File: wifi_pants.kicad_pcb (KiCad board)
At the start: 2 copper layers, 65 x 30 mm, 77 parts, among them P1 CONN_02X20, U1 ESP-12E

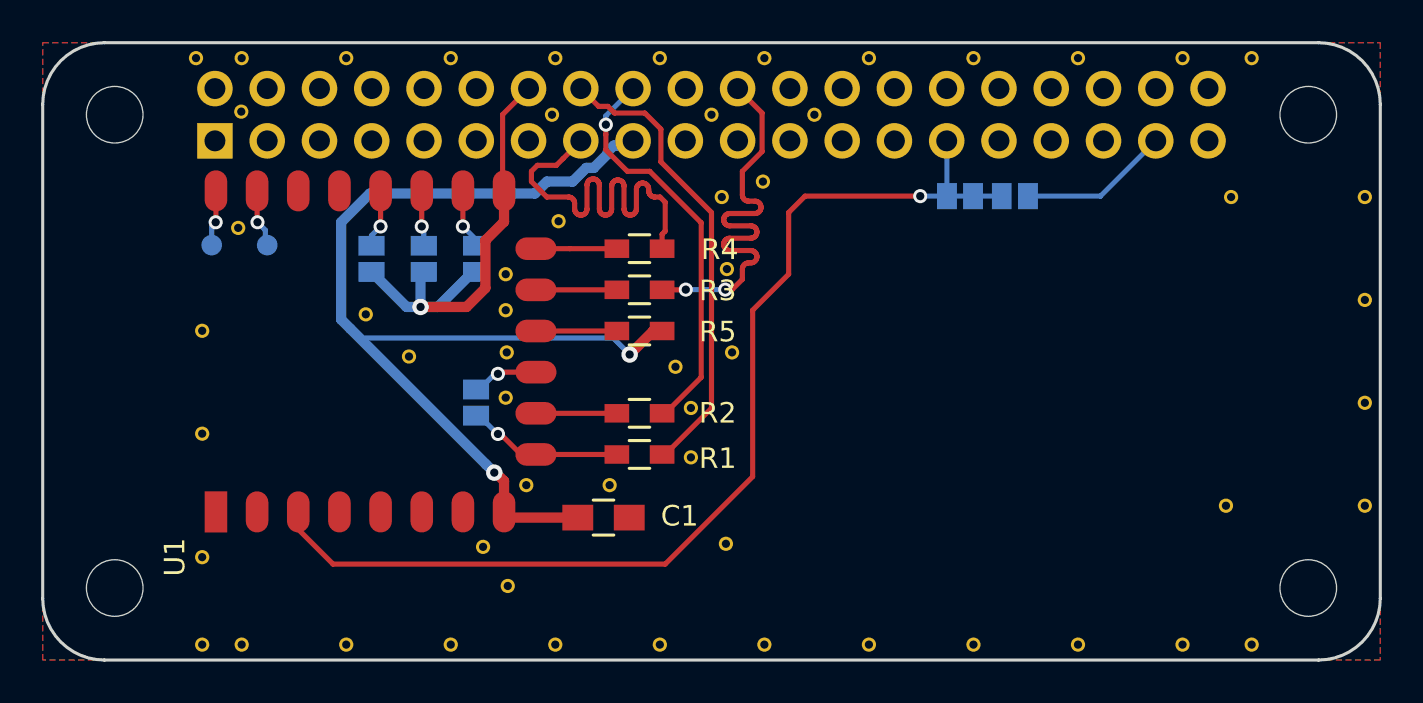
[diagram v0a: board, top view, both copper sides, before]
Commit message: Add UART header, clean up routing
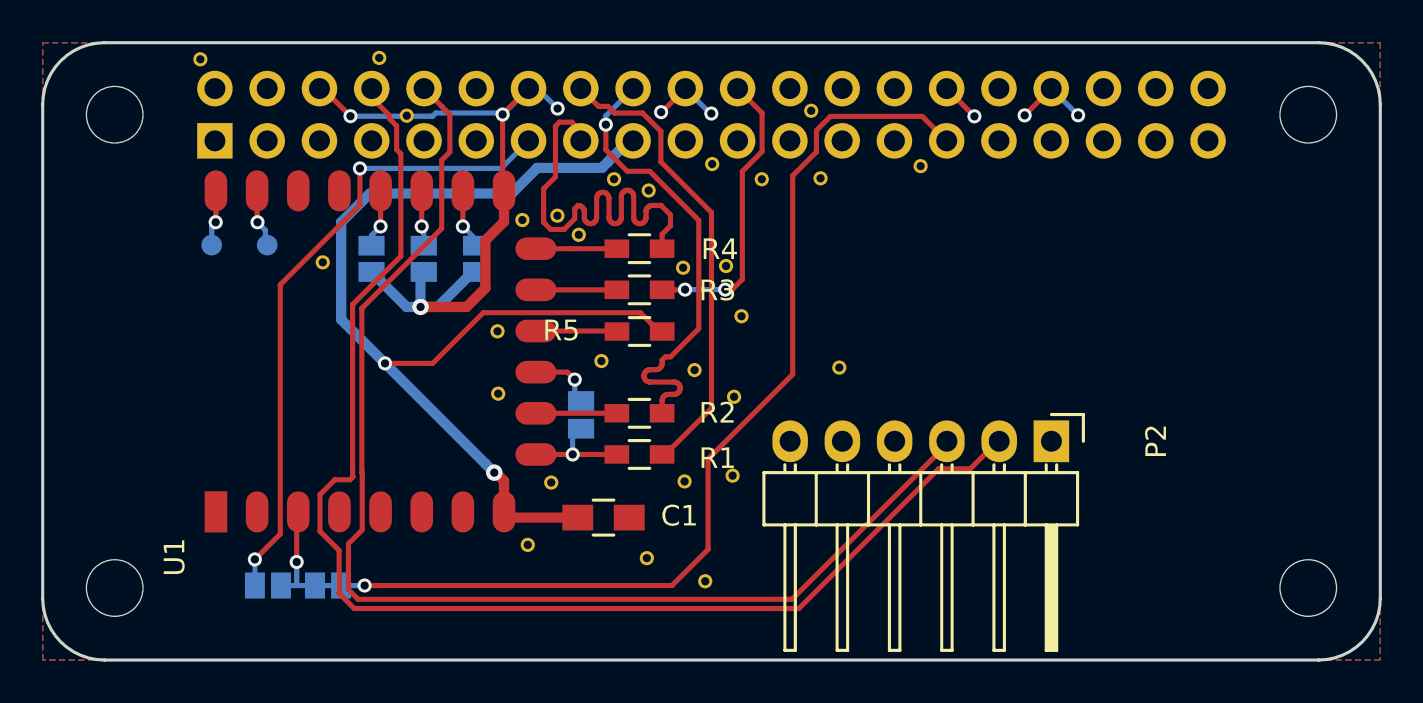
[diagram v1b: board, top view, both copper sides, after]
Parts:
- removed the REF** at (86.4, 109.5)
- removed the REF** at (87.5, 102.2)
- removed the REF** at (87.5, 98.0)
- removed the REF** at (87.5, 96.2)
- removed the REF** at (95.8, 100.8)
- removed the REF** at (96.5, 105.2)
- removed the REF** at (98.5, 100.0)
- removed the REF** at (100.0, 91.8)
- removed the REF** at (98.2, 96.0)
- removed the REF** at (89.8, 88.5)
- removed the REF** at (98.0, 92.5)
- removed the REF** at (87.6, 111.4)
- removed the REF** at (102.5, 88.5)
- removed the REF** at (97.5, 88.5)
- removed the REF** at (98.2, 109.3)
- removed the REF** at (92.5, 106.5)
- removed the REF** at (87.5, 100.0)
- removed the REF** at (82.8, 100.2)
- removed the REF** at (80.7, 98.2)
- removed the REF** at (96.5, 102.8)
- removed the REF** at (88.5, 106.5)
- removed REF**11101 (x2), REF**1111 (x2), REF**11111 (x2), REF**1121 (x2), REF**1131 (x3), REF**1141 (x2), REF**1151 (x2), REF**1161 (x2), REF**1171 (x2), REF**1181 (x2), REF**1191 (x2), REF**12, REF**13 (x5), REF**14 (x6), REF**15: VIA_0.40mm, wifi_pants:VIA_0.40mm
- added P2: CONN_01X06, Pin_Headers:Pin_Header_Angled_1x06, F.Cu at (114.0, 104.4)
- added REF**: VIA_0.40mm, wifi_pants:VIA_0.40mm, F.Cu at (97.2, 111.2)
- added REF**: VIA_0.40mm, wifi_pants:VIA_0.40mm, F.Cu at (81.4, 85.7)
- added REF**: VIA_0.40mm, wifi_pants:VIA_0.40mm, F.Cu at (102.3, 88.3)
- added REF**: VIA_0.40mm, wifi_pants:VIA_0.40mm, F.Cu at (99.9, 91.6)
- added REF**: VIA_0.40mm, wifi_pants:VIA_0.40mm, F.Cu at (103.7, 100.8)
- added REF**: VIA_0.40mm, wifi_pants:VIA_0.40mm, F.Cu at (91.1, 94.3)
- added REF**: VIA_0.40mm, wifi_pants:VIA_0.40mm, F.Cu at (94.4, 110.0)
- added REF**: VIA_0.40mm, wifi_pants:VIA_0.40mm, F.Cu at (98.6, 102.2)
- added REF**: VIA_0.40mm, wifi_pants:VIA_0.40mm, F.Cu at (98.5, 106.0)
- added REF**: VIA_0.40mm, wifi_pants:VIA_0.40mm, F.Cu at (96.2, 106.3)
- added REF**: VIA_0.40mm, wifi_pants:VIA_0.40mm, F.Cu at (89.7, 106.4)
- added REF**: VIA_0.40mm, wifi_pants:VIA_0.40mm, F.Cu at (82.7, 88.5)
- added REF**: VIA_0.40mm, wifi_pants:VIA_0.40mm, F.Cu at (87.1, 102.1)
- added REF**: VIA_0.40mm, wifi_pants:VIA_0.40mm, F.Cu at (87.1, 99.0)
- added REF**: VIA_0.40mm, wifi_pants:VIA_0.40mm, F.Cu at (88.3, 93.6)
- added REF**: VIA_0.40mm, wifi_pants:VIA_0.40mm, F.Cu at (96.7, 100.9)
- added REF**: VIA_0.40mm, wifi_pants:VIA_0.40mm, F.Cu at (97.5, 90.9)
- added REF**: VIA_0.40mm, wifi_pants:VIA_0.40mm, F.Cu at (98.2, 95.9)
- added REF**: VIA_0.40mm, wifi_pants:VIA_0.40mm, F.Cu at (94.4, 92.2)
- added REF**: VIA_0.40mm, wifi_pants:VIA_0.40mm, F.Cu at (90.0, 93.4)
- added REF**: VIA_0.40mm, wifi_pants:VIA_0.40mm, F.Cu at (92.8, 91.6)
- added REF**: VIA_0.40mm, wifi_pants:VIA_0.40mm, F.Cu at (96.1, 95.9)
- added REF**: VIA_0.40mm, wifi_pants:VIA_0.40mm, F.Cu at (78.6, 95.7)
- added REF**: VIA_0.40mm, wifi_pants:VIA_0.40mm, F.Cu at (99.0, 98.3)
- added REF**: VIA_0.40mm, wifi_pants:VIA_0.40mm, F.Cu at (92.2, 100.5)
- added REF**: VIA_0.40mm, wifi_pants:VIA_0.40mm, F.Cu at (88.6, 109.4)
- added REF**: VIA_0.40mm, wifi_pants:VIA_0.40mm, F.Cu at (107.7, 91.0)
- added REF**: VIA_0.40mm, wifi_pants:VIA_0.40mm, F.Cu at (102.8, 91.6)
- added REF**: VIA_0.40mm, wifi_pants:VIA_0.40mm, F.Cu at (72.7, 85.8)
- JP2: value Jumper_NC_Small -> Jumper_NO_Small
- moved JP1 40.9 mm to (75.9, 111.4)
- moved JP2 36.1 mm to (78.9, 111.4)
- moved JP3 5.14 mm to (91.2, 103.1), turned to 0 degrees
- turned R5 to 180 degrees
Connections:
- JP1 pad 1: GPIO5 -> GPIO27
- JP1 pad 2: GPIO26 -> GPIO5
- JP3 pad 1: //HOLD -> //CS
- JP3 pad 2: //CS -> //HOLD
- P1 pad 10: (no net) -> PI_UART0_RXD
- P1 pad 13: (no net) -> GPIO27
- P1 pad 37: GPIO26 -> (no net)
- P1 pad 8: (no net) -> PI_UART0_TXD
- R5 pad 1: //WP -> +3V3
- R5 pad 2: +3V3 -> //WP
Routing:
- net PI_UART0_TXD: track 0.00 -> 63.3 mm
- net PI_UART0_RXD: track 0.00 -> 59.5 mm
- net GPIO27: track 0.00 -> 31.1 mm, vias 0 -> 2
- net GND: track 22.5 -> 44.8 mm, vias 1 -> 9
- net GPIO26: track 7.32 -> 0.00 mm
- net SD_D1: track 21.0 -> 14.3 mm
- net GPIO5: track 52.1 -> 55.4 mm, vias 1 -> 2
- net SD_D0: track 19.8 -> 22.5 mm
- net SD_CLK: track 21.0 -> 22.5 mm
- net //CS: track 7.62 -> 6.80 mm
- net +3V3: track 54.4 -> 53.6 mm
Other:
- board text removed: "CHIP_EN SELECT"
- board text removed: "GPIO26"
- board text removed: "GPIO5"

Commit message: Add audio and expanded header
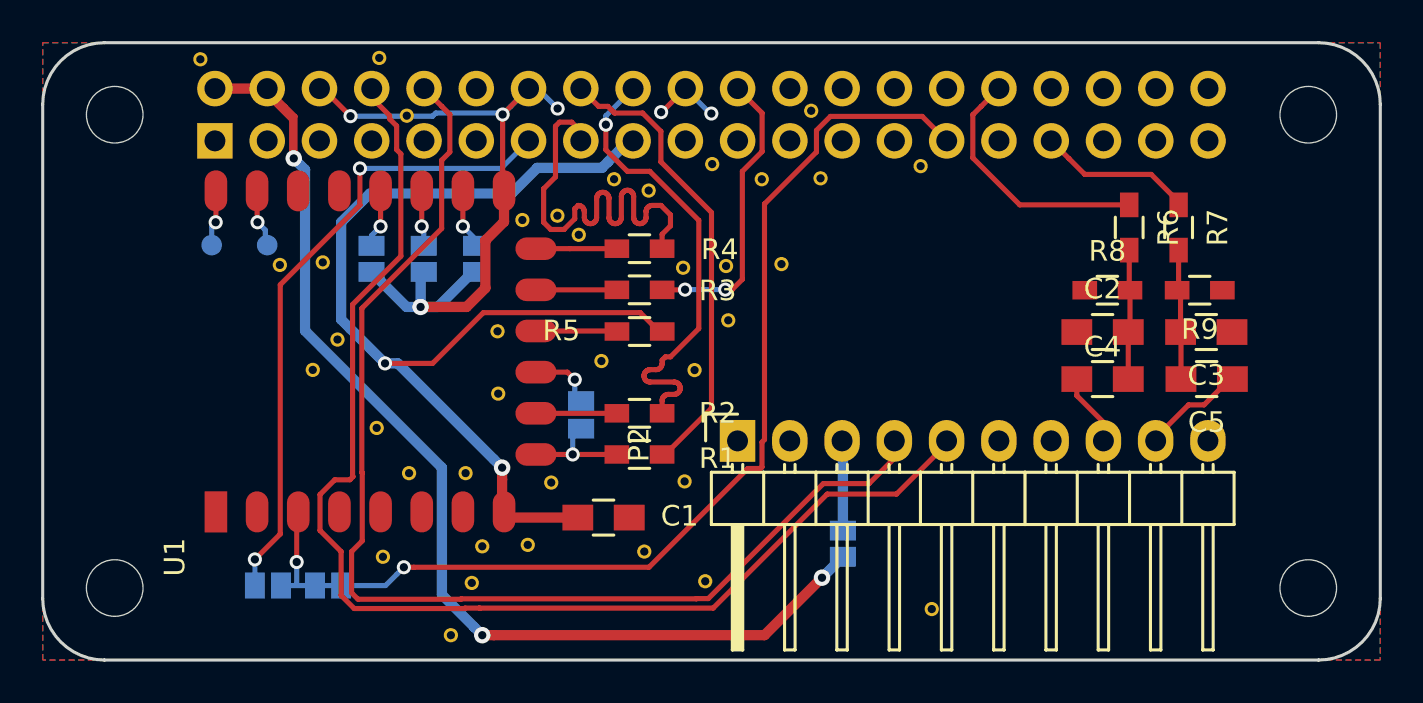
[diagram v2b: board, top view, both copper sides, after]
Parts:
- removed the REF** at (103.7, 100.8)
- removed the REF** at (98.6, 102.2)
- removed the REF** at (98.5, 106.0)
- added C2: 33nF, Capacitors_SMD:C_0805_HandSoldering, F.Cu at (116.5, 99.1)
- added C3: 33nF, Capacitors_SMD:C_0805_HandSoldering, F.Cu at (121.5, 99.1)
- added C4: 10uF, Capacitors_SMD:C_0805_HandSoldering, F.Cu at (116.5, 101.3)
- added C5: 10uF, Capacitors_SMD:C_0805_HandSoldering, F.Cu at (121.6, 101.3)
- added JP7: Jumper_NO_Small, wifi_pants:GS2, B.Cu at (103.9, 109.3)
- added R6: 270, Resistors_SMD:R_0603_HandSoldering, F.Cu at (117.8, 94.0)
- added R7: 270, Resistors_SMD:R_0603_HandSoldering, F.Cu at (120.2, 94.0)
- added R8: 150, Resistors_SMD:R_0603_HandSoldering, F.Cu at (116.7, 97.0)
- added R9: 150, Resistors_SMD:R_0603_HandSoldering, F.Cu at (121.2, 97.0)
- added REF**: VIA_0.40mm, wifi_pants:VIA_0.40mm, F.Cu at (85.9, 111.3)
- added REF**: VIA_0.40mm, wifi_pants:VIA_0.40mm, F.Cu at (76.5, 95.8)
- added REF**: VIA_0.40mm, wifi_pants:VIA_0.40mm, F.Cu at (79.3, 99.4)
- added REF**: VIA_0.40mm, wifi_pants:VIA_0.40mm, F.Cu at (100.9, 95.8)
- added REF**: VIA_0.40mm, wifi_pants:VIA_0.40mm, F.Cu at (81.5, 110.0)
- added REF**: VIA_0.40mm, wifi_pants:VIA_0.40mm, F.Cu at (84.8, 113.8)
- added REF**: VIA_0.40mm, wifi_pants:VIA_0.40mm, F.Cu at (108.2, 112.5)
- added REF**: VIA_0.40mm, wifi_pants:VIA_0.40mm, F.Cu at (81.2, 103.7)
- added REF**: VIA_0.40mm, wifi_pants:VIA_0.40mm, F.Cu at (82.8, 105.9)
- added REF**: VIA_0.40mm, wifi_pants:VIA_0.40mm, B.Cu at (86.4, 109.5)
- added REF**: VIA_0.40mm, wifi_pants:VIA_0.40mm, F.Cu at (85.5, 105.9)
- added REF**: VIA_0.40mm, wifi_pants:VIA_0.40mm, F.Cu at (78.1, 100.9)
- P2: value CONN_01X06 -> CONN_01X10; footprint Pin_Headers:Pin_Header_Angled_1x06 -> wifi_pants:Pin_Header_Angled_1x10_mirror
- moved P2 14.9 mm to (99.1, 104.5), turned to 90 degrees
- moved REF** 0.67 mm to (98.3, 98.5)
- moved REF** 0.34 mm to (94.2, 109.7)
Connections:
- P1 pad 2: (no net) -> +5V
- P1 pad 32: (no net) -> PWM0_DAC_R
- P1 pad 33: (no net) -> PWM1_DAC_L
- P1 pad 4: (no net) -> +5V
- P2 pad 1: (no net) -> GND
- P2 pad 2: PI_UART0_TXD -> (no net)
- P2 pad 3: PI_UART0_RXD -> Net-(JP7-Pad1)
- P2 pad 4: (no net) -> PI_UART0_RXD
- P2 pad 5: (no net) -> PI_UART0_TXD
- P2 pad 6: GND -> (no net)
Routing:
- net +5V: track 0.00 -> 56.8 mm, vias 0 -> 3
- net PWM0_DAC_R: track 0.00 -> 12.4 mm
- net PWM1_DAC_L: track 0.00 -> 7.57 mm
- net Net-(C2-Pad2): track 0.00 -> 6.58 mm
- net Net-(C3-Pad2): track 0.00 -> 6.37 mm
- net GND: track 44.8 -> 39.2 mm, vias 9 -> 6
- net Net-(C5-Pad1): track 0.00 -> 5.06 mm
- net Net-(JP7-Pad1): track 0.00 -> 4.39 mm
- net Net-(C4-Pad1): track 0.00 -> 3.54 mm
- net PI_UART0_TXD: track 63.3 -> 61.1 mm
- net PI_UART0_RXD: track 59.5 -> 57.4 mm
- net GPIO5: track 55.4 -> 54.6 mm

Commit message: Stitch edge, start cleaning up
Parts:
- added REF**: VIA_0.40mm, wifi_pants:VIA_0.40mm, F.Cu at (78.7, 113.9)
- added REF**: VIA_0.40mm, wifi_pants:VIA_0.40mm, F.Cu at (73.0, 97.0)
- added REF**: VIA_0.40mm, wifi_pants:VIA_0.40mm, F.Cu at (73.0, 100.0)
- added REF**: VIA_0.40mm, wifi_pants:VIA_0.40mm, F.Cu at (73.0, 103.0)
- added REF**: VIA_0.40mm, wifi_pants:VIA_0.40mm, F.Cu at (73.0, 106.0)
- added REF**: VIA_0.40mm, wifi_pants:VIA_0.40mm, F.Cu at (73.0, 110.0)
- added REF**: VIA_0.40mm, wifi_pants:VIA_0.40mm, F.Cu at (73.0, 114.0)
- added REF**: VIA_0.40mm, wifi_pants:VIA_0.40mm, F.Cu at (122.8, 97.9)
- added REF**: VIA_0.40mm, wifi_pants:VIA_0.40mm, F.Cu at (112.8, 97.9)
- added REF**: VIA_0.40mm, wifi_pants:VIA_0.40mm, F.Cu at (115.3, 88.6)
- added REF**: VIA_0.40mm, wifi_pants:VIA_0.40mm, F.Cu at (112.7, 88.6)
- added REF**: VIA_0.40mm, wifi_pants:VIA_0.40mm, F.Cu at (87.5, 96.1)
- added REF**: VIA_0.40mm, wifi_pants:VIA_0.40mm, F.Cu at (115.1, 92.3)
- added REF**: VIA_0.40mm, wifi_pants:VIA_0.40mm, F.Cu at (117.8, 103.1)
- added REF**: VIA_0.40mm, wifi_pants:VIA_0.40mm, F.Cu at (117.8, 98.3)
- added REF**: VIA_0.40mm, wifi_pants:VIA_0.40mm, F.Cu at (99.6, 112.6)
- added REF**: VIA_0.40mm, wifi_pants:VIA_0.40mm, F.Cu at (101.4, 114.2)
- added REF**: VIA_0.40mm, wifi_pants:VIA_0.40mm, F.Cu at (123.2, 86.0)
- added REF**: VIA_0.40mm, wifi_pants:VIA_0.40mm, F.Cu at (129.0, 91.8)
- added REF**: VIA_0.40mm, wifi_pants:VIA_0.40mm, F.Cu at (129.0, 108.0)
- added REF**: VIA_0.40mm, wifi_pants:VIA_0.40mm, F.Cu at (123.5, 114.0)
- added REF**: VIA_0.40mm, wifi_pants:VIA_0.40mm, F.Cu at (74.7, 88.4)
- moved REF** 9.14 mm to (101.7, 106.2)
- moved C2 1.24 mm to (115.3, 99.4)
- moved C3 1.24 mm to (120.3, 99.4)
- moved C4 1.24 mm to (115.3, 101.6), turned to 180 degrees
- moved R6 1.24 mm to (116.6, 94.3)
- moved R7 1.24 mm to (119.0, 94.3)
- moved R8 1.24 mm to (115.5, 97.3)
- moved R9 1.24 mm to (120.0, 97.3)
- moved C5 1.24 mm to (120.4, 101.6), turned to 0 degrees
- moved REF** 0.78 mm to (98.9, 98.0)
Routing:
- net GND: track 39.2 -> 43.4 mm
- net Net-(C5-Pad1): track 5.06 -> 2.87 mm
- net Net-(C3-Pad2): track 6.37 -> 7.83 mm
- net PWM0_DAC_R: track 12.4 -> 11.2 mm
- net Net-(C2-Pad2): track 6.58 -> 7.48 mm

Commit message: Add audio, change header to include audio and +5V in, cleanup silk
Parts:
- removed the REF** at (87.1, 102.1)
- added REF**: VIA_0.40mm, wifi_pants:VIA_0.40mm, F.Cu at (72.4, 93.4)
- added REF**: VIA_0.40mm, wifi_pants:VIA_0.40mm, F.Cu at (86.8, 103.5)
- added REF**: VIA_0.40mm, wifi_pants:VIA_0.40mm, F.Cu at (101.1, 102.4)
- added REF**: VIA_0.40mm, wifi_pants:VIA_0.40mm, F.Cu at (90.1, 102.0)
- added REF**: VIA_0.40mm, wifi_pants:VIA_0.40mm, F.Cu at (90.1, 104.0)
- JP1: value Jumper_NO_Small -> 27
- JP2: value Jumper_NO_Small -> 5
- JP7: value Jumper_NO_Small -> EXT_5V
- W5: value TXD -> ESP_TXD
- W6: value RXD -> ESP_RXD
- moved JP3 2.54 mm to (88.6, 103.1)
- moved REF** 0.65 mm to (102.0, 114.2)
- renumbered R5 to R3, R3 to R4, R4 to R5
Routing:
- net //HOLD: track 3.86 -> 3.13 mm
- net GPIO27: track 31.1 -> 31.7 mm
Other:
- board text added: "-"
- board text added: "5V IN"
- board text added: "AUDIO L"
- board text added: "AUDIO R"
- board text added: "CHIP_EN SEL"
- board text added: "ESP-12E or ESP-12F"
- board text added: "GND"
- board text added: "PI RXD"
- board text added: "PI TXD"
- board text removed: "ESP8266 WiFi Pants for Raspberry Pi v0.1 2016-01-12 by Andrew Litt https://github.com/al177/wifi_pants"

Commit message: Add logo
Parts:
- added G***: LOGO, wifi_pants:pants_logo, B.Cu at (76.6, 105.2)
- added REF**: VIA_0.40mm, wifi_pants:VIA_0.40mm, F.Cu at (106.3, 98.0)
- added REF**: VIA_0.40mm, wifi_pants:VIA_0.40mm, F.Cu at (105.3, 107.8)
- added REF**: VIA_0.40mm, wifi_pants:VIA_0.40mm, F.Cu at (108.9, 106.5)
- added REF**: VIA_0.40mm, wifi_pants:VIA_0.40mm, F.Cu at (117.8, 105.7)
- added REF**: Symbol_OSHW-Logo_SilkScreen, Symbols:Symbol_OSHW-Logo_SilkScreen, F.Cu at (106.3, 98.0)
- moved REF** 2.29 mm to (83.4, 103.1)
- moved REF** 0.70 mm to (83.5, 106.1)
- moved REF** 0.38 mm to (77.9, 100.6)
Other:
- board text added: "CHIP_EN"
- board text added: "WiFi Pants"
- board text added: "github.com/al177 /wifi_pants"
- board text removed: "CHIP_EN SEL"

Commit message: Order r1, check in r1 gerbers
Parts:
- added REF**: VIA_0.40mm, wifi_pants:VIA_0.40mm, F.Cu at (79.2, 109.8)
- moved REF** 0.22 mm to (79.3, 99.2)
- moved REF** 0.18 mm to (78.6, 95.8)
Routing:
- net +3V3: track 53.7 -> 52.4 mm
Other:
- board text added: "r1"
